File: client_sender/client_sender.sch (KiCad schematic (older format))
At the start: 16 parts, among them P1 CONN_01X06, P2 CONN_01X08, SW1 DIPS_08, SW2 SW_PUSH, SW3 SW_PUSH, U1 ESP-12_Breakout, U2 MCP23017, U3 MCP3208, U4 WS2812B

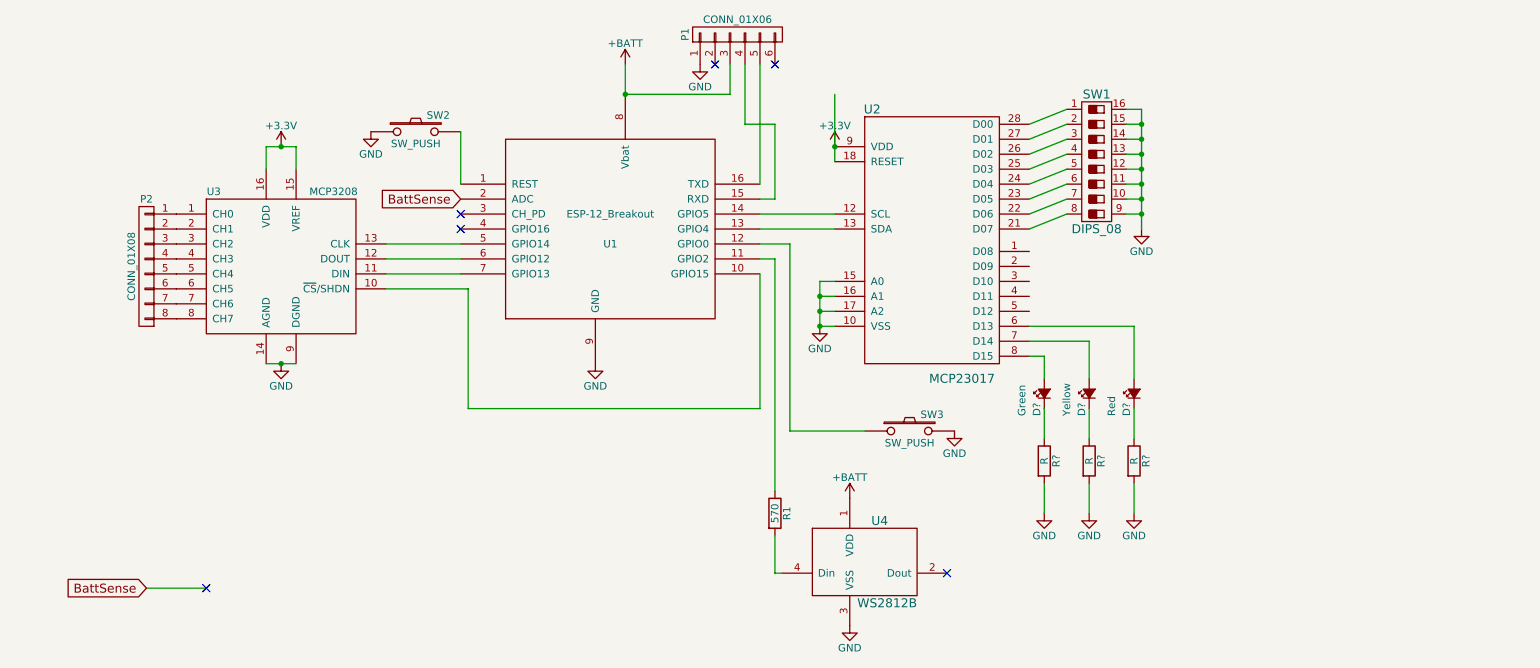
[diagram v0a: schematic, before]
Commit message: minor tweaks to schematic + RENAMED ALL FILES
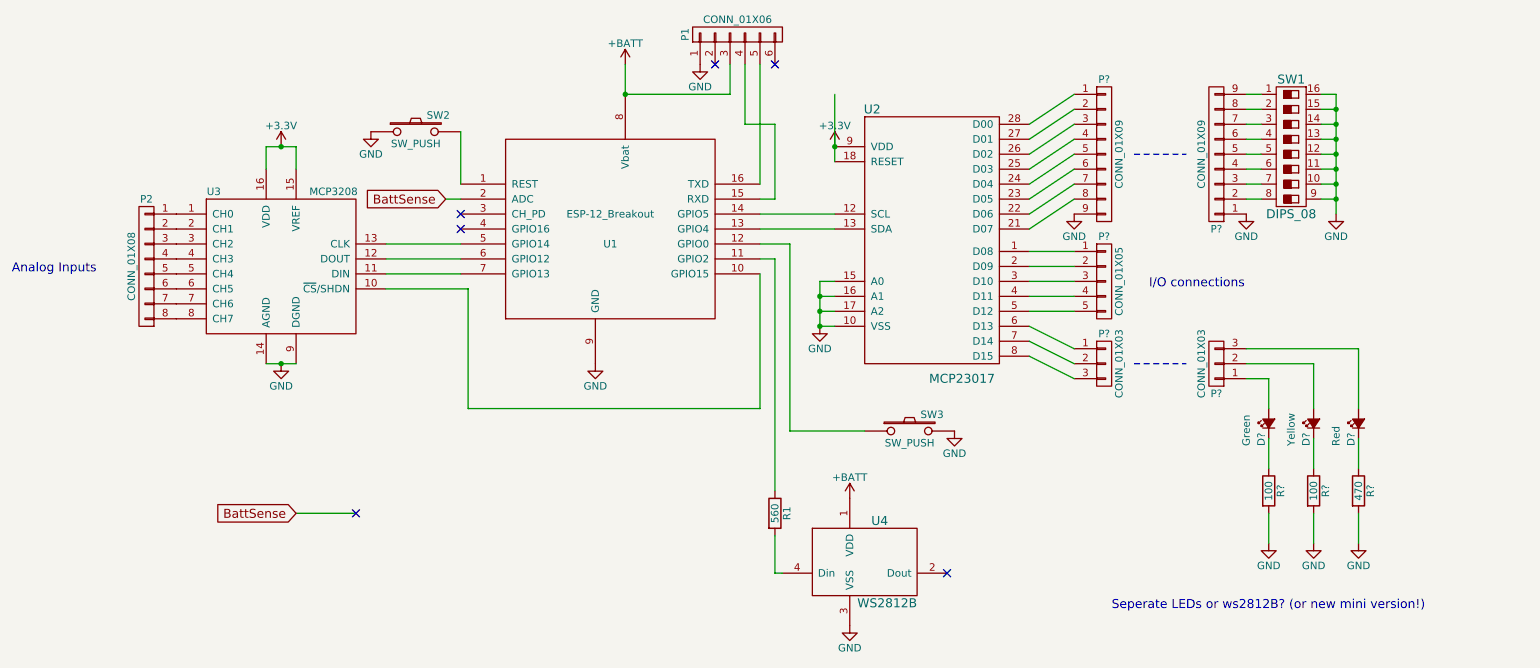
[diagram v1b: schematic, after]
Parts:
- added P? (x2): CONN_01X09, symbol CONN_01X09
- added P? (x2): CONN_01X03, symbol CONN_01X03
- added P?: CONN_01X05, symbol CONN_01X05
- R1: value 570 -> 560
- R? (x2): value R -> 100
- R?: value R -> 470
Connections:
- net GND: now also P?.1 (P1), P?.9 (P9)
- net at SW1.1: now also P?.9 (P9); no longer U2.28 (D00)
- net at SW1.2: now also P?.8 (P8); no longer U2.27 (D01)
- net at SW1.3: now also P?.7 (P7); no longer U2.26 (D02)
- net at SW1.4: now also P?.6 (P6); no longer U2.25 (D03)
- net at SW1.5: now also P?.5 (P5); no longer U2.24 (D04)
- net at SW1.6: now also P?.4 (P4); no longer U2.23 (D05)
- net at SW1.7: now also P?.3 (P3); no longer U2.22 (D06)
- net at SW1.8: now also P?.2 (P2); no longer U2.21 (D07)
- net at U2.1 (D08): now also P?.1 (P1)
- net at U2.2 (D09): now also P?.2 (P2)
- net at U2.3 (D10): now also P?.3 (P3)
- net at U2.4 (D11): now also P?.4 (P4)
- net at U2.5 (D12): now also P?.5 (P5)
- net at U2.6 (D13): now also P?.1 (P1); no longer D?.2 (A)
- net at U2.7 (D14): now also P?.2 (P2); no longer D?.2 (A)
- net at U2.8 (D15): now also P?.3 (P3); no longer D?.2 (A)
- new net: P?.8 (P8), U2.21 (D07)
- new net: P?.7 (P7), U2.22 (D06)
- new net: P?.6 (P6), U2.23 (D05)
- new net: P?.5 (P5), U2.24 (D04)
- new net: P?.4 (P4), U2.25 (D03)
- new net: P?.3 (P3), U2.26 (D02)
- new net: P?.2 (P2), U2.27 (D01)
- new net: P?.1 (P1), U2.28 (D00)
- new net: D?.2 (A), P?.2 (P2)
- new net: D?.2 (A), P?.1 (P1)
- new net: D?.2 (A), P?.3 (P3)
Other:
- note added: "Analog Inputs"
- note added: "I/O connections"
- note added: "Seperate LEDs or ws2812B? (or new mini version!)"
- moved on the sheet: D?, R?, SW1
